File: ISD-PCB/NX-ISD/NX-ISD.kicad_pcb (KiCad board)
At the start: 4 copper layers, 77 x 48.6 mm, 105 parts, among them J1 1-2328702-0, J2 UJ20-C-H-G-SMT-1-P16-TR, P1 S2B-PH-SM4-TB, Q1 AO3400A, Q2 AO3401A, Q3 BC847W, Q4 AO3400A, U1 ESP32-S3-WROOM-1, U10 BNO085, U11 PCA9306, U12 OPT3001DNPR, U13 RT9193-18GB, U14 ZDSD02GLGEAG, U15 USBLC6-2P6, U16 TXB0106RGY, U2 TLV62568DBV, U3 MAX17048G_T10, U4 RV-3028-C7, U5 MAX30102, U6 BME690, U7 TM-2025A, U8 BQ25170DSGR, U9 RT9193-28GB, Y2 32.768

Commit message: v1p3 production ready
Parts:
- added ?: , , F.Cu at (179.4, 83.9)
- added REF**: TestPoint_Plated_Hole_D2.0mm, TestPoint:TestPoint_Plated_Hole_D2.0mm, F.Cu at (179.4, 122.7)
- added REF**: TestPoint_Plated_Hole_D2.0mm, TestPoint:TestPoint_Plated_Hole_D2.0mm, F.Cu at (132.2, 116.7)
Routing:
- net /Logic section/BTN: track 21.8 -> 22.5 mm
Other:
- outline, holes or cut-outs redrawn
- board text added: "JLCPCB production settings: Additional settings after uploading the .zip gerber folder: PCB-Thickness: 1.2mm (I personally recommand staying between 1.2mm and 1.6mm) Material Type: FR4-TG155 (Important!) Surface finish: ENIG (Essential for these small pads) Gold Thickness: 1 U{dblquote} Min via hole size/diameter: 0.25mm/(0.35/0.4mm) (4-Kelvin test should be automatically selected) Optional setti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"

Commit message: v1p3 - updated final circuit
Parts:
- R15: value 220 -> 10
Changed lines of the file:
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@@
 		(sheetname "/Peripherie/")
 		(sheetfile "peripherie.kicad_sch")
+		(units
+			(unit
+				(name "A")
+				(pins "4" "3" "2" "1")
+			)
+		)
 		(attr smd)
 		(duplicate_pad_numbers_are_jumpers no)
@@
 		(sheetname "/Peripherie/")
 		(sheetfile "peripherie.kicad_sch")
+		(units
+			(unit
+				(name "A")
+				(pins "4" "3" "2" "1")
+			)
+		)
 		(attr smd)
 		(duplicate_pad_numbers_are_jumpers no)
@@
 		(sheetname "/Peripherie/")
 		(sheetfile "peripherie.kicad_sch")
+		(units
+			(unit
+				(name "A")
+				(pins "4" "3" "2" "1")
+			)
+		)
 		(attr smd)
 		(duplicate_pad_numbers_are_jumpers no)
@@
 			)
 		)
-		(property "Value" "220"
+		(property "Value" "10"
 			(at 0 1.17 90)
 			(layer "F.Fab")
@@
 		(sheetname "/Peripherie/")
 		(sheetfile "peripherie.kicad_sch")
+		(units
+			(unit
+				(name "A")
+				(pins "4" "3" "2" "1")
+			)
+		)
 		(attr smd)
 		(duplicate_pad_numbers_are_jumpers no)
@@
 		(sheetname "/Sersor section/")
 		(sheetfile "sensor_section.kicad_sch")
+		(units
+			(unit
+				(name "A")
+				(pins "1" "4" "6" "5" "2" "7" "3")
+			)
+		)
 		(attr smd)
 		(duplicate_pad_numbers_are_jumpers no)
@@
 		(sheetname "/Peripherie/")
 		(sheetfile "peripherie.kicad_sch")
+		(units
+			(unit
+				(name "A")
+				(pins "4" "3" "2" "1")
+			)
+		)
 		(attr smd)
 		(duplicate_pad_numbers_are_jumpers no)
@@
 		(sheetname "/Peripherie/")
 		(sheetfile "peripherie.kicad_sch")
+		(units
+			(unit
+				(name "A")
+				(pins "4" "3" "2" "1")
+			)
+		)
 		(attr smd)
 		(duplicate_pad_numbers_are_jumpers no)
@@
 		(sheetname "/Peripherie/")
 		(sheetfile "peripherie.kicad_sch")
+		(units
+			(unit
+				(name "A")
+				(pins "4" "3" "2" "1")
+			)
+		)
 		(attr smd)
 		(duplicate_pad_numbers_are_jumpers no)

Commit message: v1p3 - Isssues fixed
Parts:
- added C27: 100n, Capacitor_SMD:C_0402_1005Metric, F.Cu at (149.1, 93.6)
- added R16: 10k, Resistor_SMD:R_0402_1005Metric, F.Cu at (179.7, 95.8)
- added R17: 10k, Resistor_SMD:R_0402_1005Metric, F.Cu at (179.7, 97.1)
- added R20: 51.1k, Resistor_SMD:R_0402_1005Metric, F.Cu at (148.7, 89.8)
- added R22: 51.1k, Resistor_SMD:R_0402_1005Metric, F.Cu at (147.7, 93.6)
- C2: value 1u -> 4.7u
- R21: value 4.7k -> 51.1k
- R9: renamed from R2; value 220 -> 1k
- U13: renamed from U1; value ESP32-S3-WROOM-1 -> ESP32-S3-WROOM-1_N16R8
- Y1: renamed from Y2; value 32.768 -> 32.768 kHz
- moved R21 26.3 mm to (158.0, 95.0), turned to 0 degrees
- renumbered C13 to C1, C21 to C10, C22 to C11, C2 to C12, C1 to C13, C5 to C14, C18 to C15, C4 to C16, C7 to C17, C12 to C18, C30 to C19, C19 to C2, C6 to C20, C29 to C21, C28 to C22, C27 to C23, C16 to C24, C17 to C25, C8 to C26, C25 to C28, C24 to C29, C14 to C3, C15 to C4, C9 to C5, C23 to C6, C11 to C7, C10 to C8, C20 to C9, D5 to D1, D1 to D2, D2 to D3, G7 to G10, G15 to G12, G4 to G13, G8 to G14, G12 to G15, G5 to G2, G9 to G3, G13 to G4, G2 to G5, G10 to G7, G14 to G8, G3 to G9, J2 to J1, J1 to J2, Q3 to Q1, Q1 to Q3, R9 to R1, R6 to R10, R23 to R11, R22 to R12, R18 to R13, R19 to R14, R24 to R15, R17 to R18, R3 to R19, R1 to R2, R5 to R23, R4 to R24, R10 to R25, R14 to R26, R15 to R27, R16 to R3, R20 to R4, R8 to R5, R11 to R6, R13 to R7, R12 to R8, U13 to U1, U12 to U10, U10 to U11, U4 to U12, U16 to U15, U7 to U16, U15 to U2, U2 to U3, U9 to U4, U8 to U5, U3 to U6, U6 to U7, U5 to U8, U11 to U9
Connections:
- R21 pad 1: /Logic section/!INT_HR -> +3V3
- R21 pad 2: +1V8 -> /Logic section/CS_SD
- RN1 pad 3: /Logic section/!ALERT -> /Logic section/!INT_HR
- U11 pad 15: unconnected-(U10-ENV_SCL-Pad15) -> Net-(U11-ENV_SCL)
- U11 pad 16: unconnected-(U10-ENV_SDA-Pad16) -> Net-(U11-ENV_SDA)
- U8 pad 10: unconnected-(U5-VLED+-Pad10) -> +3V3
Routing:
- net /Logic section/!ALERT: track 111.6 -> 90.0 mm, vias 3 -> 2
- net +3V3: track 50.6 -> 57.0 mm, vias 37 -> 41
- net /Logic section/!INT_HR: track 78.9 -> 85.2 mm
- net /Logic section/CS_SD: track 30.8 -> 34.8 mm
- net Net-(U11-ENV_SCL): track 0.00 -> 3.23 mm
- net Net-(U11-ENV_SDA): track 0.00 -> 2.64 mm
- net /Logic section/!INT_RTC: track 79.7 -> 77.8 mm
- net /Logic section/MOSI: track 43.5 -> 42.3 mm
- net /Logic section/MISO: track 7.75 -> 6.71 mm
- net +1V8: track 9.18 -> 8.19 mm, vias 7 -> 6
- net GND: track 106.9 -> 107.7 mm, vias 102 -> 103

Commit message: v1p3 - fixed
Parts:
- removed the C2 at (147.5, 111.7)
- C14: value 100n -> 1u; footprint Capacitor_SMD:C_0402_1005Metric -> Capacitor_SMD:C_0603_1608Metric
- TH1: value 10k -> 10k NTC
- moved C14 0.64 mm to (183.7, 110.2), turned to 135 degrees
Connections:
- ? pad 1: (no net) -> GND
- REF** pad 1: (no net) -> GND (x2)
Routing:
- net VBAT: track 23.0 -> 20.9 mm
- net GND: track 107.7 -> 106.0 mm, vias 103 -> 102

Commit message: v1p3 - HRM Cap fix &more
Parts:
- removed C14: 1u, Capacitor_SMD:C_0603_1608Metric
- removed C15: 100n, Capacitor_SMD:C_0402_1005Metric
- added C30: 100n, Capacitor_SMD:C_0402_1005Metric, F.Cu at (184.7, 110.5)
- added C31: 100n, Capacitor_SMD:C_0402_1005Metric, F.Cu at (183.1, 112.0)
- added C32: 4.7u, Capacitor_SMD:C_0603_1608Metric, F.Cu at (181.8, 110.5)
- added C33: 10u, Capacitor_SMD:C_0603_1608Metric, F.Cu at (183.1, 109.2)
- U13: value ESP32-S3-WROOM-1_N16R8 -> ESP32-S3-WROOM-1-N16R8
- moved G*** 0.70 mm to (187.9, 108.1)
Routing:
- net +3V3: track 56.9 -> 53.6 mm, vias 41 -> 42
- net +1V8: track 8.19 -> 5.56 mm
- net GND: track 106.0 -> 107.6 mm, vias 102 -> 104
- net /Logic section/SCL_1: track 133.9 -> 132.3 mm
- net /Logic section/!INT_HR: track 85.2 -> 85.1 mm, vias 2 -> 4

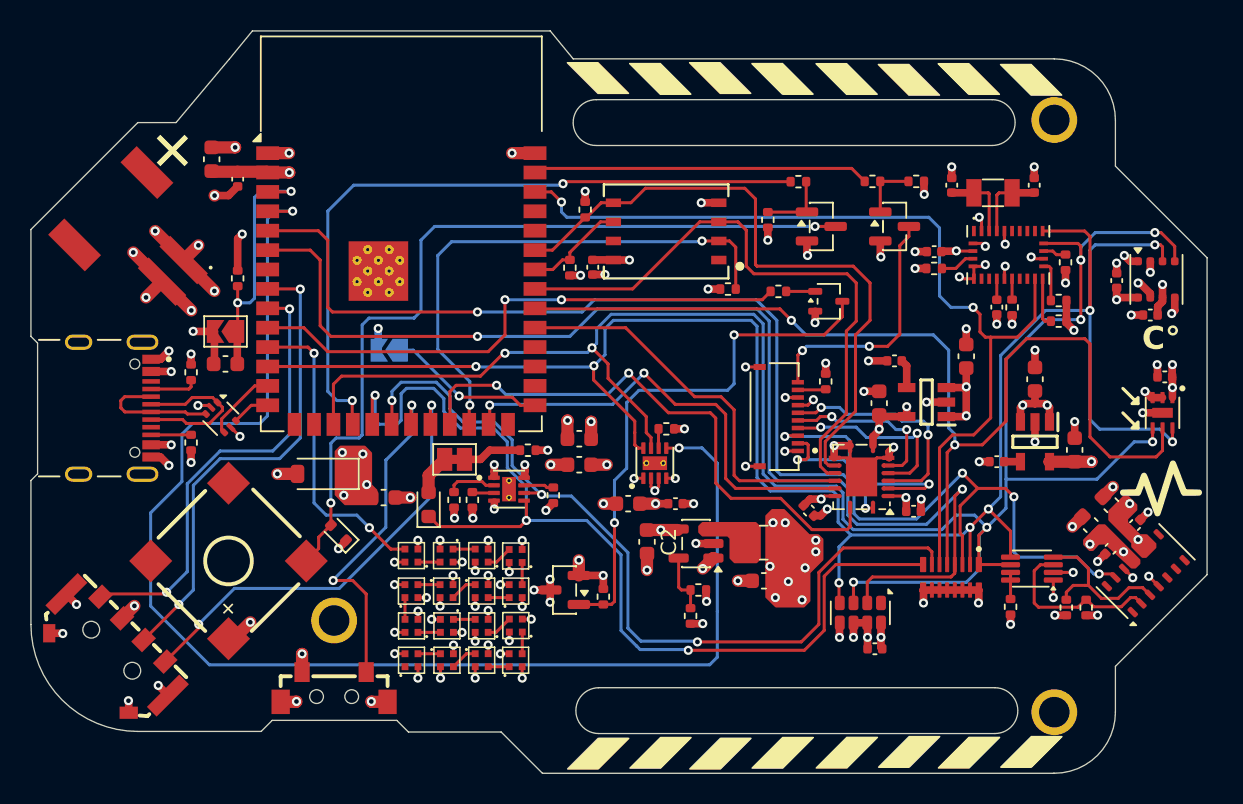
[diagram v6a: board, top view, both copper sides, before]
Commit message: v1p3 - RTC fix
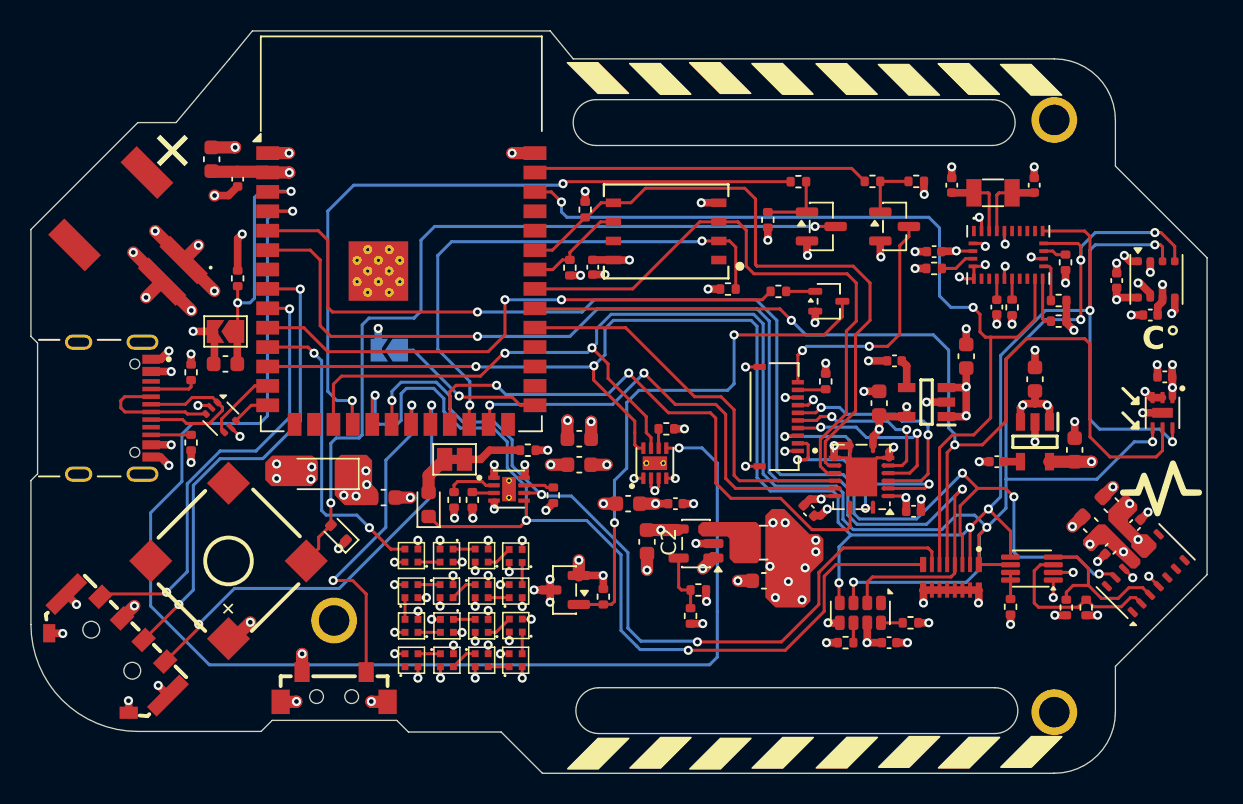
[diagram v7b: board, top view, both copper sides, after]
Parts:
- added R28: 10k, Resistor_SMD:R_0402_1005Metric, F.Cu at (165.7, 118.2)
- added R29: 10k, Resistor_SMD:R_0402_1005Metric, F.Cu at (169.9, 116.8)
- moved C20 1.01 mm to (168.6, 118.2)
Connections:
- U12 pad 6: +3V3 -> Net-(U12-VBACKUP)
- U12 pad 8: GND -> Net-(U12-EVI)
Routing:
- net Net-(U12-EVI): track 0.00 -> 1.42 mm
- net /Power section/USB_P: track 4.80 -> 3.48 mm, vias 4 -> 7
- net Net-(U12-VBACKUP): track 0.00 -> 1.30 mm
- net +3V3: track 53.6 -> 52.3 mm, vias 42 -> 41
- net /Logic section/USB_DETECT: track 55.9 -> 55.1 mm
- net /Logic section/BAT_STAT: track 67.0 -> 66.3 mm
- net /Logic section/LEVER_PUSH: track 31.6 -> 31.0 mm
- net /Logic section/LEVER_RIGHT: track 29.8 -> 29.2 mm
- net GND: track 107.6 -> 107.8 mm, vias 104 -> 106
